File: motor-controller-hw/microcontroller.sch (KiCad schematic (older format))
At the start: 28 parts, among them U201 STM32F303RETx

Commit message: Moving away from TMC4671
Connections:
- net labels added: AGND, GNDA
- wire segments 171 -> 173
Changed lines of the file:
@@
 	4800 4850 4900 4850
 Wire Wire Line
-	5200 4850 5200 4750
-Wire Wire Line
 	5100 4750 5100 4850
-Connection ~ 5100 4850
-Wire Wire Line
-	5100 4850 5200 4850
 Wire Wire Line
 	5000 4750 5000 4850
@@
 $EndComp
 $Comp
-L MotorControllerParts:GNDD #PWR?
-U 1 1 5BF507B6
-P 3050 7600
-F 0 "#PWR?" H 3050 7350 50  0001 C CNN
-F 1 "GNDD" H 3054 7445 50  0000 C CNN
-F 2 "" H 3050 7600 50  0001 C CNN
-F 3 "" H 3050 7600 50  0001 C CNN
-	1    3050 7600
-	1    0    0    -1
-$EndComp
-$Comp
 L motor-controller-hw-cache:+3.3V #PWR?
 U 1 1 5BF50827
@@
 L MotorControllerParts:GNDD #PWR?
 U 1 1 5BF58438
-P 1250 3050
-F 0 "#PWR?" H 1250 2800 50  0001 C CNN
-F 1 "GNDD" H 1254 2895 50  0000 C CNN
-F 2 "" H 1250 3050 50  0001 C CNN
-F 3 "" H 1250 3050 50  0001 C CNN
-	1    1250 3050
-	1    0    0    -1
-$EndComp
-Wire Wire Line
-	1250 3050 1250 2950
-Wire Wire Line
-	1250 2950 1150 2950
+P 1550 3200
+F 0 "#PWR?" H 1550 2950 50  0001 C CNN
+F 1 "GNDD" H 1554 3045 50  0000 C CNN
+F 2 "" H 1550 3200 50  0001 C CNN
+F 3 "" H 1550 3200 50  0001 C CNN
+	1    1550 3200
+	1    0    0    -1
+$EndComp
+Wire Wire Line
+	1550 3200 1550 2950
+Wire Wire Line
+	1550 2950 1150 2950
 $Comp
 L MotorControllerParts:+3.3V #PWR?
@@
 Wire Wire Line
 	2850 5200 3250 5200
+Text HLabel 1150 3050 0    50   Input ~ 0
+AGND
+$Comp
+L MotorControllerParts:GNDA #PWR?
+U 1 1 5C4A865C
+P 1300 3200
+F 0 "#PWR?" H 1300 2950 50  0001 C CNN
+F 1 "GNDA" H 1305 3027 50  0000 C CNN
+F 2 "" H 1300 3200 50  0001 C CNN
+F 3 "" H 1300 3200 50  0001 C CNN
+	1    1300 3200
+	1    0    0    -1
+$EndComp
+Wire Wire Line
+	1300 3200 1300 3050
+Wire Wire Line
+	1300 3050 1150 3050
+Wire Wire Line
+	5200 4850 5200 4750
+Wire Wire Line
+	5200 4850 5100 4850
+Connection ~ 5100 4850
+$Comp
+L MotorControllerParts:GNDD #PWR?
+U 1 1 5C8CD47C
+P 3050 7600
+F 0 "#PWR?" H 3050 7350 50  0001 C CNN
+F 1 "GNDD" H 3054 7445 50  0000 C CNN
+F 2 "" H 3050 7600 50  0001 C CNN
+F 3 "" H 3050 7600 50  0001 C CNN
+	1    3050 7600
+	1    0    0    -1
+$EndComp
 $EndSCHEMATC

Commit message: Voltage regualtor changes, name changes, and HANDS!!!
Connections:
- net labels added: TMC4671_EN, TMC4671_Status, TMC_4671_En_In
- net labels removed: AGND, GNDA
- wire segments 173 -> 175
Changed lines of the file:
@@
 Wire Wire Line
 	2850 5200 3250 5200
-Text HLabel 1150 3050 0    50   Input ~ 0
-AGND
-$Comp
-L MotorControllerParts:GNDA #PWR?
-U 1 1 5C4A865C
-P 1300 3200
-F 0 "#PWR?" H 1300 2950 50  0001 C CNN
-F 1 "GNDA" H 1305 3027 50  0000 C CNN
-F 2 "" H 1300 3200 50  0001 C CNN
-F 3 "" H 1300 3200 50  0001 C CNN
-	1    1300 3200
-	1    0    0    -1
-$EndComp
-Wire Wire Line
-	1300 3200 1300 3050
-Wire Wire Line
-	1300 3050 1150 3050
 Wire Wire Line
 	5200 4850 5200 4750
@@
 	1    0    0    -1
 $EndComp
+Text HLabel 9700 1000 2    50   Output ~ 0
+TMC4671_EN
+Text Label 9000 1000 0    50   ~ 0
+TMC_4671_En_In
+Wire Wire Line
+	9700 1000 9000 1000
+Text HLabel 9700 1100 2    50   Input ~ 0
+TMC4671_Status
+Text Label 9000 1100 0    50   ~ 0
+TMC4671_Status
+Wire Wire Line
+	9700 1100 9000 1100
+Text Label 6400 4150 2    50   ~ 0
+TMC4671_Status
+Text Label 6400 4050 2    50   ~ 0
+TMC_4671_En_In
+Wire Wire Line
+	6400 4050 5700 4050
+Wire Wire Line
+	6400 4150 5700 4150
 $EndSCHEMATC

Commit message: Working schematics
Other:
- moved on the sheet: U201

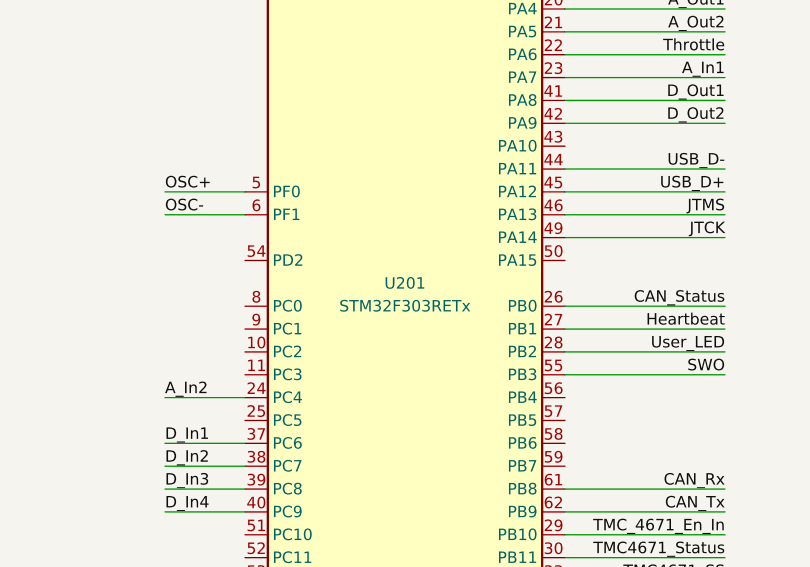
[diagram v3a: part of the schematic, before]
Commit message: Compacted schematic layout
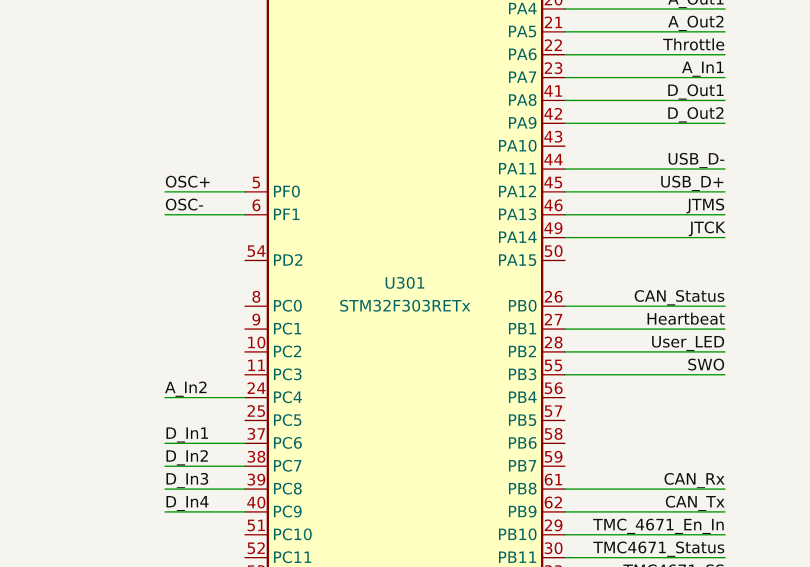
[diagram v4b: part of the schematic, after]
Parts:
- gave numbers to parts that had none: 27
- renumbered U201 to U301

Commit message: Moved all parts into the MotorControllerParts.lib file
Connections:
- net labels added: SPI_MISO, SPI_MOSI, SPI_SCK, SPI_SS, ~SPI_SS
- wire segments 175 -> 183
- no-connect marks 0 -> 12
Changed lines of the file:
@@
 	8100 5750 7450 5750
 Connection ~ 7450 5750
-Text Label 4350 2600 0    50   ~ 0
+Text Label 4300 2600 0    50   ~ 0
 OSC-
-Text Label 4350 2500 0    50   ~ 0
+Text Label 4300 2500 0    50   ~ 0
 OSC+
 Wire Wire Line
-	4350 2500 4700 2500
-Wire Wire Line
-	4350 2600 4700 2600
+	4300 2500 4700 2500
+Wire Wire Line
+	4300 2600 4700 2600
 Text Notes 6450 5550 0    50   ~ 0
 Crystal Oscilator with 18pf load capacitor rating.\nAssumed stray capacitance of 5pf.\nSee: https://www.allaboutcircuits.com/technical-articles/\nchoosing-the-right-oscillator-for-your-microcontroller/
@@
 Text Label 6800 2000 2    50   ~ 0
 A_In1
-Text Label 4350 3400 0    50   ~ 0
+Text Label 4300 3400 0    50   ~ 0
 A_In2
 Wire Wire Line
 	6800 2000 6100 2000
 Wire Wire Line
-	4350 3400 4700 3400
+	4300 3400 4700 3400
 Text Label 6800 1900 2    50   ~ 0
 Throttle
@@
 Text Label 1550 2350 2    50   ~ 0
 D_In4
-Text Label 4350 3600 0    50   ~ 0
+Text Label 4300 3600 0    50   ~ 0
 D_In1
-Text Label 4350 3700 0    50   ~ 0
+Text Label 4300 3700 0    50   ~ 0
 D_In2
-Text Label 4350 3800 0    50   ~ 0
+Text Label 4300 3800 0    50   ~ 0
 D_In3
-Text Label 4350 3900 0    50   ~ 0
+Text Label 4300 3900 0    50   ~ 0
 D_In4
 Wire Wire Line
-	4350 3600 4700 3600
-Wire Wire Line
-	4350 3700 4700 3700
-Wire Wire Line
-	4350 3800 4700 3800
-Wire Wire Line
-	4350 3900 4700 3900
+	4300 3600 4700 3600
+Wire Wire Line
+	4300 3700 4700 3700
+Wire Wire Line
+	4300 3800 4700 3800
+Wire Wire Line
+	4300 3900 4700 3900
 Wire Wire Line
 	1550 2050 1150 2050
@@
 Wire Wire Line
 	1050 5800 1300 5800
-Text Label 4350 1500 0    50   ~ 0
+Text Label 4300 1500 0    50   ~ 0
 Boot
 Wire Wire Line
-	4350 1500 4700 1500
-Text Label 4350 1300 0    50   ~ 0
+	4300 1500 4700 1500
+Text Label 4300 1300 0    50   ~ 0
 Reset
 Wire Wire Line
-	4350 1300 4700 1300
+	4300 1300 4700 1300
 $Comp
 L MotorControllerParts:LED_ALT D301
@@
 U 1 1 5C12B80C
 P 10100 4350
-F 0 "SW303" V 10050 4350 50  0000 R CNN
-F 1 "User_SW" V 10250 4550 50  0000 R CNN
+F 0 "SW303" V 10250 4500 50  0000 R CNN
+F 1 "User_SW" V 10350 4550 50  0000 R CNN
 F 2 "" H 10100 4350 50  0001 C CNN
 F 3 "" H 10100 4350 50  0001 C CNN
@@
 Wire Wire Line
 	9650 3850 9650 3900
-Text Label 4350 4300 0    50   ~ 0
+Text Label 4300 4300 0    50   ~ 0
 User_SW
 Wire Wire Line
-	4350 4300 4700 4300
+	4300 4300 4700 4300
 Text Label 9000 4250 0    50   ~ 0
 User_SW
 Wire Wire Line
 	9000 4250 9650 4250
-Text HLabel 9700 1350 2    50   Output ~ 0
+Text HLabel 9700 1650 2    50   Output ~ 0
 ~TMC4671_SS
+Text HLabel 9700 1550 2    50   Output ~ 0
+TMC4671_SCK
+Text HLabel 9700 1350 2    50   Input ~ 0
+TMC4671_MISO
 Text HLabel 9700 1450 2    50   Output ~ 0
+TMC4671_MOSI
+Text Label 9000 1450 0    50   ~ 0
+TMC4671_MOSI
+Text Label 9000 1350 0    50   ~ 0
+TMC4671_MISO
+Text Label 9000 1550 0    50   ~ 0
 TMC4671_SCK
-Text HLabel 9700 1650 2    50   Input ~ 0
-TMC4671_MISO
-Text HLabel 9700 1550 2    50   Output ~ 0
-TMC4671_MOSI
-Text Label 9000 1550 0    50   ~ 0
-TMC4671_MOSI
 Text Label 9000 1650 0    50   ~ 0
-TMC4671_MISO
-Text Label 9000 1450 0    50   ~ 0
-TMC4671_SCK
-Text Label 9000 1350 0    50   ~ 0
 TMC4671_SS
 Wire Wire Line
+	9000 1450 9700 1450
+Wire Wire Line
+	9000 1350 9700 1350
+Wire Wire Line
 	9000 1550 9700 1550
 Wire Wire Line
 	9000 1650 9700 1650
-Wire Wire Line
-	9000 1450 9700 1450
-Wire Wire Line
-	9000 1350 9700 1350
 Wire Notes Line
 	8900 2650 10400 2650
@@
 Wire Wire Line
 	6800 4100 6100 4100
+Text Label 4300 4200 0    50   ~ 0
+SPI_MOSI
+Text Label 4300 4100 0    50   ~ 0
+SPI_MISO
+Text Label 4300 4000 0    50   ~ 0
+SPI_SCK
+Text Label 6800 2800 2    50   ~ 0
+SPI_SS
+Wire Wire Line
+	6800 2800 6100 2800
+Wire Wire Line
+	4300 4200 4700 4200
+Wire Wire Line
+	4300 4100 4700 4100
+Wire Wire Line
+	4300 4000 4700 4000
+Text HLabel 9700 2200 2    50   Output ~ 0
+~SPI_SS
+Text HLabel 9700 2100 2    50   Output ~ 0
+SPI_SCK
+Text HLabel 9700 1900 2    50   Input ~ 0
+SPI_MISO
+Text HLabel 9700 2000 2    50   Output ~ 0
+SPI_MOSI
+Wire Wire Line
+	9000 2000 9700 2000
+Wire Wire Line
+	9000 1900 9700 1900
+Wire Wire Line
+	9000 2100 9700 2100
+Wire Wire Line
+	9000 2200 9700 2200
+Text Label 9000 1900 0    50   ~ 0
+SPI_MISO
+Text Label 9000 2000 0    50   ~ 0
+SPI_MOSI
+Text Label 9000 2100 0    50   ~ 0
+SPI_SCK
+Text Label 9000 2200 0    50   ~ 0
+SPI_SS
+NoConn ~ 6100 3700
+NoConn ~ 6100 3600
+NoConn ~ 6100 3500
+NoConn ~ 6100 3400
+NoConn ~ 4700 4500
+NoConn ~ 4700 3500
+NoConn ~ 4700 3300
+NoConn ~ 4700 3200
+NoConn ~ 4700 3100
+NoConn ~ 4700 3000
+NoConn ~ 4700 2800
+NoConn ~ 4700 4400
 $EndSCHEMATC

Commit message: Added footprints, changed pdf
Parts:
- C301, C302, C303, C304, C305, C306, C307, C308, C309, C310, C311: footprint (none) -> Capacitor_SMD:C_0805_2012Metric_Pad1.15x1.40mm_HandSolder
- J301: footprint (none) -> Connector_PinHeader_2.54mm:PinHeader_1x06_P2.54mm_Vertical
- J302: footprint (none) -> Connector_PinHeader_2.54mm:PinHeader_1x03_P2.54mm_Vertical
- R301, R302, R303, R304, R305, R306, R307: footprint (none) -> Resistor_SMD:R_0805_2012Metric_Pad1.15x1.40mm_HandSolder
- Y301: footprint (none) -> Crystal:Crystal_SMD_HC49-SD_HandSoldering
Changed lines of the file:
@@
 F 0 "C301" H 950 7350 50  0000 L CNN
 F 1 "100n" H 950 7150 50  0000 L CNN
-F 2 "" H 938 7100 50  0001 C CNN
+F 2 "Capacitor_SMD:C_0805_2012Metric_Pad1.15x1.40mm_HandSolder" H 938 7100 50  0001 C CNN
 F 3 "~" H 900 7250 50  0001 C CNN
 	1    900  7250
@@
 F 0 "C302" H 1300 7350 50  0000 L CNN
 F 1 "100n" H 1300 7150 50  0000 L CNN
-F 2 "" H 1288 7100 50  0001 C CNN
+F 2 "Capacitor_SMD:C_0805_2012Metric_Pad1.15x1.40mm_HandSolder" H 1288 7100 50  0001 C CNN
 F 3 "~" H 1250 7250 50  0001 C CNN
 	1    1250 7250
@@
 F 0 "C304" H 1650 7350 50  0000 L CNN
 F 1 "100n" H 1650 7150 50  0000 L CNN
-F 2 "" H 1638 7100 50  0001 C CNN
+F 2 "Capacitor_SMD:C_0805_2012Metric_Pad1.15x1.40mm_HandSolder" H 1638 7100 50  0001 C CNN
 F 3 "~" H 1600 7250 50  0001 C CNN
 	1    1600 7250
@@
 F 0 "C305" H 2000 7350 50  0000 L CNN
 F 1 "100n" H 2000 7150 50  0000 L CNN
-F 2 "" H 1988 7100 50  0001 C CNN
+F 2 "Capacitor_SMD:C_0805_2012Metric_Pad1.15x1.40mm_HandSolder" H 1988 7100 50  0001 C CNN
 F 3 "~" H 1950 7250 50  0001 C CNN
 	1    1950 7250
@@
 F 0 "C306" H 2350 7350 50  0000 L CNN
 F 1 "4u7" H 2350 7150 50  0000 L CNN
-F 2 "" H 2338 7100 50  0001 C CNN
+F 2 "Capacitor_SMD:C_0805_2012Metric_Pad1.15x1.40mm_HandSolder" H 2338 7100 50  0001 C CNN
 F 3 "~" H 2300 7250 50  0001 C CNN
 	1    2300 7250
@@
 F 0 "C308" H 3250 7350 50  0000 L CNN
 F 1 "10n" H 3250 7150 50  0000 L CNN
-F 2 "" H 3238 7100 50  0001 C CNN
+F 2 "Capacitor_SMD:C_0805_2012Metric_Pad1.15x1.40mm_HandSolder" H 3238 7100 50  0001 C CNN
 F 3 "~" H 3200 7250 50  0001 C CNN
 	1    3200 7250
@@
 F 0 "C307" H 2950 7350 50  0000 L CNN
 F 1 "1u" H 2950 7150 50  0000 L CNN
-F 2 "" H 2938 7100 50  0001 C CNN
+F 2 "Capacitor_SMD:C_0805_2012Metric_Pad1.15x1.40mm_HandSolder" H 2938 7100 50  0001 C CNN
 F 3 "~" H 2900 7250 50  0001 C CNN
 	1    2900 7250
@@
 F 0 "Y301" V 7450 5800 50  0000 C CNN
 F 1 "8Mhz" V 7600 5850 50  0000 C CNN
-F 2 "" H 7450 6000 50  0001 C CNN
+F 2 "Crystal:Crystal_SMD_HC49-SD_HandSoldering" H 7450 6000 50  0001 C CNN
 F 3 "~" H 7450 6000 50  0001 C CNN
 	1    7450 6000
@@
 F 0 "C309" V 7200 5550 50  0000 L CNN
 F 1 "26pf" V 7350 5650 50  0000 L CNN
-F 2 "" H 7250 5750 50  0001 C CNN
+F 2 "Capacitor_SMD:C_0805_2012Metric_Pad1.15x1.40mm_HandSolder" H 7250 5750 50  0001 C CNN
 F 3 "~" H 7250 5750 50  0001 C CNN
 	1    7250 5750
@@
 F 0 "C310" V 7200 6050 50  0000 L CNN
 F 1 "26pf" V 7350 6150 50  0000 L CNN
-F 2 "" H 7250 6250 50  0001 C CNN
+F 2 "Capacitor_SMD:C_0805_2012Metric_Pad1.15x1.40mm_HandSolder" H 7250 6250 50  0001 C CNN
 F 3 "~" H 7250 6250 50  0001 C CNN
 	1    7250 6250
@@
 F 0 "R302" V 7650 6250 50  0000 C CNN
 F 1 "390R" V 7850 6250 50  0000 C CNN
-F 2 "" H 7750 6250 50  0001 C CNN
+F 2 "Resistor_SMD:R_0805_2012Metric_Pad1.15x1.40mm_HandSolder" H 7750 6250 50  0001 C CNN
 F 3 "~" H 7750 6250 50  0001 C CNN
 	1    7750 6250
@@
 F 0 "C303" H 1350 5700 50  0000 L CNN
 F 1 "100n" H 1350 5500 50  0000 L CNN
-F 2 "" H 1338 5450 50  0001 C CNN
+F 2 "Capacitor_SMD:C_0805_2012Metric_Pad1.15x1.40mm_HandSolder" H 1338 5450 50  0001 C CNN
 F 3 "~" H 1300 5600 50  0001 C CNN
 	1    1300 5600
@@
 F 0 "R301" H 2070 5696 50  0000 L CNN
 F 1 "10K" H 2070 5605 50  0000 L CNN
-F 2 "" V 1930 5650 50  0001 C CNN
+F 2 "Resistor_SMD:R_0805_2012Metric_Pad1.15x1.40mm_HandSolder" V 1930 5650 50  0001 C CNN
 F 3 "~" H 2000 5650 50  0001 C CNN
 	1    2000 5650
@@
 F 0 "J301" H 3530 5392 50  0000 L CNN
 F 1 "SWD" H 3530 5301 50  0000 L CNN
-F 2 "" H 3450 5400 50  0001 C CNN
+F 2 "Connector_PinHeader_2.54mm:PinHeader_1x06_P2.54mm_Vertical" H 3450 5400 50  0001 C CNN
 F 3 "~" H 3450 5400 50  0001 C CNN
 	1    3450 5400
@@
 F 0 "R307" V 10050 6300 50  0000 C CNN
 F 1 "510R" V 9834 6300 50  0000 C CNN
-F 2 "" V 9880 6300 50  0001 C CNN
+F 2 "Resistor_SMD:R_0805_2012Metric_Pad1.15x1.40mm_HandSolder" V 9880 6300 50  0001 C CNN
 F 3 "~" H 9950 6300 50  0001 C CNN
 	1    9950 6300
@@
 F 0 "R306" V 10050 5900 50  0000 C CNN
 F 1 "510R" V 9834 5900 50  0000 C CNN
-F 2 "" V 9880 5900 50  0001 C CNN
+F 2 "Resistor_SMD:R_0805_2012Metric_Pad1.15x1.40mm_HandSolder" V 9880 5900 50  0001 C CNN
 F 3 "~" H 9950 5900 50  0001 C CNN
 	1    9950 5900
@@
 F 0 "R305" V 10050 5500 50  0000 C CNN
 F 1 "510R" V 9834 5500 50  0000 C CNN
-F 2 "" V 9880 5500 50  0001 C CNN
+F 2 "Resistor_SMD:R_0805_2012Metric_Pad1.15x1.40mm_HandSolder" V 9880 5500 50  0001 C CNN
 F 3 "~" H 9950 5500 50  0001 C CNN
 	1    9950 5500
@@
 F 0 "C311" H 9765 4496 50  0000 L CNN
 F 1 "100n" H 9765 4405 50  0000 L CNN
-F 2 "" H 9688 4300 50  0001 C CNN
+F 2 "Capacitor_SMD:C_0805_2012Metric_Pad1.15x1.40mm_HandSolder" H 9688 4300 50  0001 C CNN
 F 3 "~" H 9650 4450 50  0001 C CNN
 	1    9650 4450
@@
 F 0 "R303" H 9720 4096 50  0000 L CNN
 F 1 "4K7" H 9720 4005 50  0000 L CNN
-F 2 "" V 9580 4050 50  0001 C CNN
+F 2 "Resistor_SMD:R_0805_2012Metric_Pad1.15x1.40mm_HandSolder" V 9580 4050 50  0001 C CNN
 F 3 "~" H 9650 4050 50  0001 C CNN
 	1    9650 4050
@@
 F 0 "R304" H 9720 4846 50  0000 L CNN
 F 1 "100R" H 9720 4755 50  0000 L CNN
-F 2 "" V 9580 4800 50  0001 C CNN
+F 2 "Resistor_SMD:R_0805_2012Metric_Pad1.15x1.40mm_HandSolder" V 9580 4800 50  0001 C CNN
 F 3 "~" H 9650 4800 50  0001 C CNN
 	1    9650 4800
@@
 F 0 "J302" H 9900 3300 50  0000 L CNN
 F 1 "User USART" H 9750 2900 50  0000 L CNN
-F 2 "" H 9950 3100 50  0001 C CNN
+F 2 "Connector_PinHeader_2.54mm:PinHeader_1x03_P2.54mm_Vertical" H 9950 3100 50  0001 C CNN
 F 3 "~" H 9950 3100 50  0001 C CNN
 	1    9950 3100

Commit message: Finished adding footprints to the schematic, started layout
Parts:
- D301, D302, D303: footprint (none) -> LED_SMD:LED_0603_1608Metric_Pad1.05x0.95mm_HandSolder
- SW301, SW302, SW303: footprint (none) -> supermileage_footprints:SW_SPST_FSMSM
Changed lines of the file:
@@
 F 0 "SW301" V 850 5550 50  0000 R CNN
 F 1 "Reset" V 1050 5750 50  0000 R CNN
-F 2 "" H 900 5550 50  0001 C CNN
+F 2 "supermileage_footprints:SW_SPST_FSMSM" H 900 5550 50  0001 C CNN
 F 3 "" H 900 5550 50  0001 C CNN
 	1    900  5550
@@
 F 0 "SW302" V 2050 5250 50  0000 R CNN
 F 1 "Boot" V 2250 5450 50  0000 R CNN
-F 2 "" H 2100 5250 50  0001 C CNN
+F 2 "supermileage_footprints:SW_SPST_FSMSM" H 2100 5250 50  0001 C CNN
 F 3 "" H 2100 5250 50  0001 C CNN
 	1    2100 5250
@@
 F 0 "D301" H 9500 5600 50  0000 C CNN
 F 1 "CAN_Status" H 9542 5336 50  0000 C CNN
-F 2 "" H 9550 5500 50  0001 C CNN
+F 2 "LED_SMD:LED_0603_1608Metric_Pad1.05x0.95mm_HandSolder" H 9550 5500 50  0001 C CNN
 F 3 "~" H 9550 5500 50  0001 C CNN
 	1    9550 5500
@@
 F 0 "D302" H 9500 6000 50  0000 C CNN
 F 1 "Heartbeat" H 9542 5736 50  0000 C CNN
-F 2 "" H 9550 5900 50  0001 C CNN
+F 2 "LED_SMD:LED_0603_1608Metric_Pad1.05x0.95mm_HandSolder" H 9550 5900 50  0001 C CNN
 F 3 "~" H 9550 5900 50  0001 C CNN
 	1    9550 5900
@@
 F 0 "D303" H 9500 6400 50  0000 C CNN
 F 1 "User_LED" H 9542 6136 50  0000 C CNN
-F 2 "" H 9550 6300 50  0001 C CNN
+F 2 "LED_SMD:LED_0603_1608Metric_Pad1.05x0.95mm_HandSolder" H 9550 6300 50  0001 C CNN
 F 3 "~" H 9550 6300 50  0001 C CNN
 	1    9550 6300
@@
 F 0 "SW303" V 10250 4500 50  0000 R CNN
 F 1 "User_SW" V 10350 4550 50  0000 R CNN
-F 2 "" H 10100 4350 50  0001 C CNN
+F 2 "supermileage_footprints:SW_SPST_FSMSM" H 10100 4350 50  0001 C CNN
 F 3 "" H 10100 4350 50  0001 C CNN
 	1    10100 4350
